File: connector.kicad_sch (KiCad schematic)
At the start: 3 parts, among them J1 PCIEx4_HOST, Q1 MMBT3904

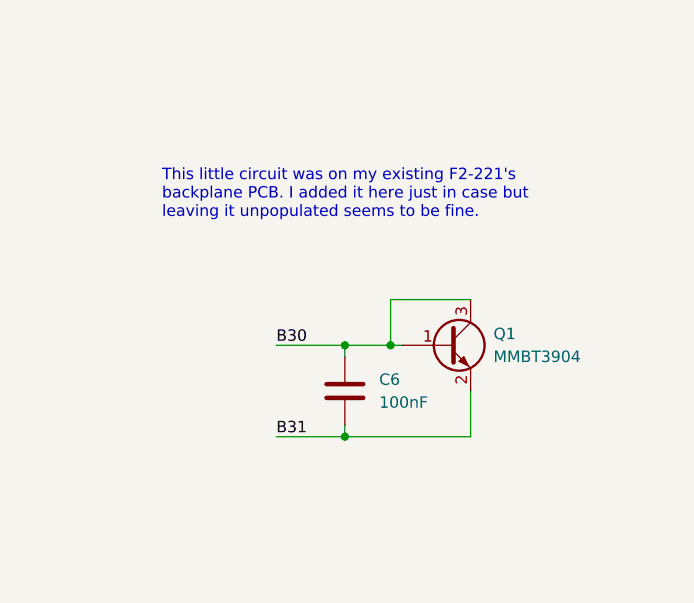
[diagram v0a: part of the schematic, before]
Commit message: no DRC errors
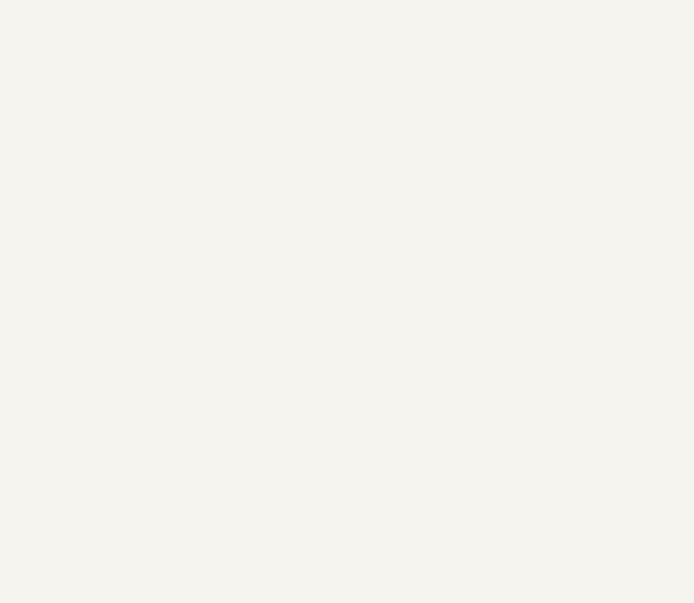
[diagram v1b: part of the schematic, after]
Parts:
- removed C6: 100nF, Capacitor_SMD:C_0603_1608Metric, symbol Device:C
- removed Q1: MMBT3904, Package_TO_SOT_SMD:SOT-23, symbol Transistor_BJT:MMBT3904
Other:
- note removed: "This little circuit was on my existing F2-221's backplane PCB. I added it here just in case but leaving it unpopulated seems to be fine."
